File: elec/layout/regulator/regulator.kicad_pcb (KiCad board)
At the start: 2 copper layers, 13 parts, among them U1 _Texas_Instruments_TPS56637RP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

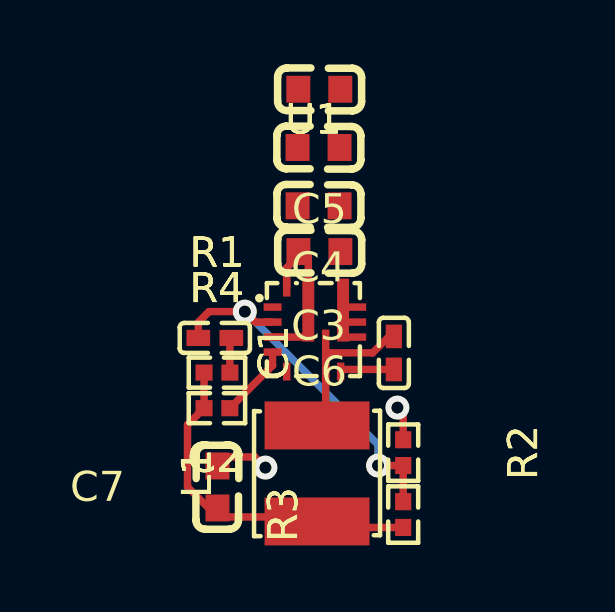
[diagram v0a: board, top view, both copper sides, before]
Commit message: Don't update PCB files
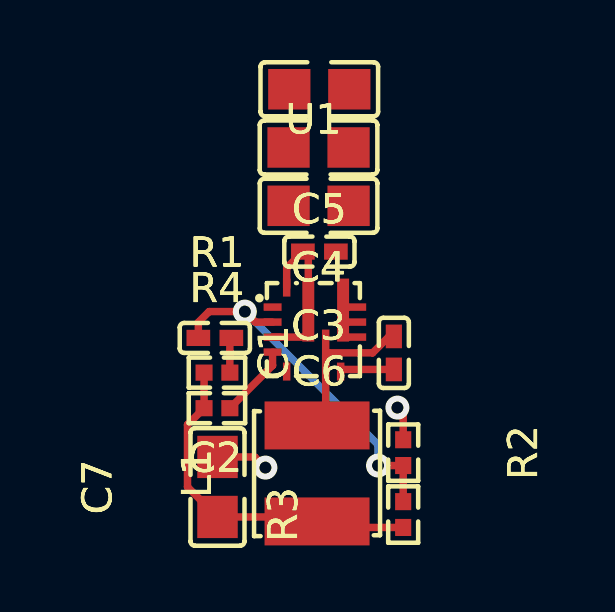
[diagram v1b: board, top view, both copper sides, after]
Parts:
- C3, C4, C5: value 100nF ±10% 50V X7R -> 4.7µF ±10% 25V X5R; footprint lcsc:C0603 -> lcsc:C0805
- C6: value 100nF ±10% 50V X7R -> 100nF ±10% 16V X7R; footprint lcsc:C0603 -> lcsc:C0402
- C7: value 100nF ±10% 50V X7R -> 47µF ±20% 6.3V X5R; footprint lcsc:C0603 -> lcsc:C0805
- L1: value 3.3µH ±20% infHz 4A 73mΩ -> 3.3µH ±20% 4A 73mΩ
- R1: value 20kΩ ±1% 62.5mW -> 22kΩ ±1% 62.5mW
- R2: value 10kΩ ±1% 62.5mW -> 8.2kΩ ±1% 62.5mW
- R3: value 75kΩ ±1% 62.5mW -> 68kΩ ±1% 62.5mW
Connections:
- C1 pad 2: net-5 -> net-6
- C2 pad 1: net -> net-4
- C2 pad 2: net-1 -> net-5
- C3 pad 1: net-2 -> net
- C3 pad 2: net-3 -> net-1
- C4 pad 1: net-2 -> net
- C4 pad 2: net-3 -> net-1
- C5 pad 1: net-2 -> net
- C5 pad 2: net-3 -> net-1
- C6 pad 1: net-2 -> net
- C6 pad 2: net-3 -> net-1
- C7 pad 1: net-4 -> net-2
- C7 pad 2: net-3 -> net-1
- L1 pad 1: net-4 -> net-2
- L1 pad 2: net-5 -> net-6
- R1 pad 1: net-4 -> net-2
- R1 pad 2: net -> net-4
- R2 pad 1: net-3 -> net-1
- R2 pad 2: net-1 -> net-5
- R3 pad 1: net-4 -> net-2
- R3 pad 2: net-1 -> net-5
- R4 pad 1: net-4 -> net-2
- R4 pad 2: net-6 -> net-3
- U1 pad 10: net-3 -> net-1
- U1 pad 2: net-1 -> net-5
- U1 pad 3: net-3 -> net-1
- U1 pad 4: net-6 -> net-3
- U1 pad 6: net-5 -> net-6
- U1 pad 8: net-2 -> net
- U1 pad 9: net-3 -> net-1

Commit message: Build full
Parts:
- C3, C4, C5: value 4.7µF ±10% 25V X5R -> 100nF ±10% 50V X7R; footprint lcsc:C0805 -> lcsc:C0603
- C6: value 100nF ±10% 16V X7R -> 100nF ±10% 50V X7R; footprint lcsc:C0402 -> lcsc:C0603
- C7: value 47µF ±20% 6.3V X5R -> 100nF ±10% 50V X7R; footprint lcsc:C0805 -> lcsc:C0603
- L1: value 3.3µH ±20% 4A 73mΩ -> 3.3µH ±20% infHz 4A 73mΩ
- R1: value 22kΩ ±1% 62.5mW -> 20kΩ ±1% 62.5mW
- R2: value 8.2kΩ ±1% 62.5mW -> 10kΩ ±1% 62.5mW
- R3: value 68kΩ ±1% 62.5mW -> 75kΩ ±1% 62.5mW
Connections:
- C1 pad 2: net-6 -> net-5
- C2 pad 1: net-4 -> net
- C2 pad 2: net-5 -> net-1
- C3 pad 1: net -> net-2
- C3 pad 2: net-1 -> net-3
- C4 pad 1: net -> net-2
- C4 pad 2: net-1 -> net-3
- C5 pad 1: net -> net-2
- C5 pad 2: net-1 -> net-3
- C6 pad 1: net -> net-2
- C6 pad 2: net-1 -> net-3
- C7 pad 1: net-2 -> net-4
- C7 pad 2: net-1 -> net-3
- L1 pad 1: net-2 -> net-4
- L1 pad 2: net-6 -> net-5
- R1 pad 1: net-2 -> net-4
- R1 pad 2: net-4 -> net
- R2 pad 1: net-1 -> net-3
- R2 pad 2: net-5 -> net-1
- R3 pad 1: net-2 -> net-4
- R3 pad 2: net-5 -> net-1
- R4 pad 1: net-2 -> net-4
- R4 pad 2: net-3 -> net-6
- U1 pad 10: net-1 -> net-3
- U1 pad 2: net-5 -> net-1
- U1 pad 3: net-1 -> net-3
- U1 pad 4: net-3 -> net-6
- U1 pad 6: net-6 -> net-5
- U1 pad 8: net -> net-2
- U1 pad 9: net-1 -> net-3
